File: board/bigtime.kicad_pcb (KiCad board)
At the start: 2 copper layers, 90 x 142 mm, 124 parts, among them IC1 NPIC6C596A, IC2 TPS62152, IC3 25AA02E48, IC4 STM32F407VET6, IC5 KSZ8081RNx, IC6 MAX5969x, IC7 MAX17503, IC8 LDL212DR, J1 RJHSE-538B, J2 MICROUSB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

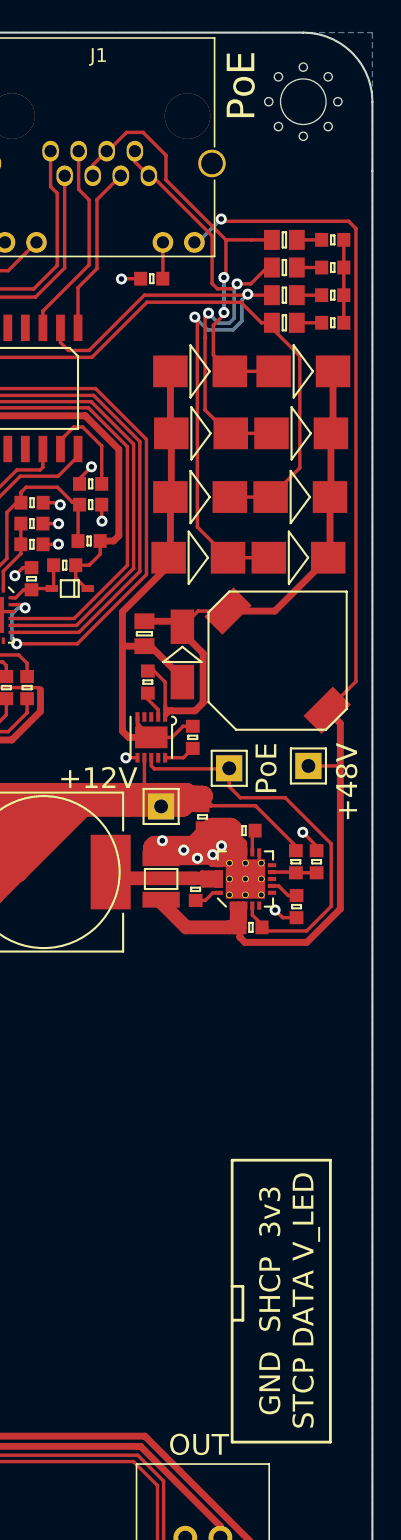
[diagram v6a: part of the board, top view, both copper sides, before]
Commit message: more silk fiddling
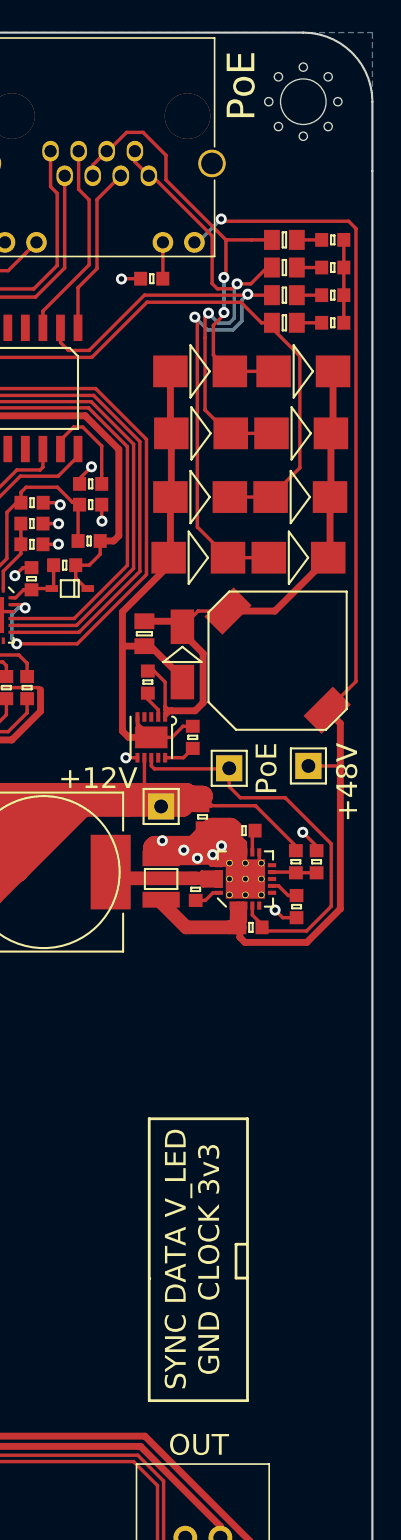
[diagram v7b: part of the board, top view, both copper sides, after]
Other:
- board text added: "SYNC DATA V_LED GND CLOCK 3v3"
- board text removed: "GND SHCP 3v3 STCP DATA V_LED"
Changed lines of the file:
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@@
     (descr "mod. jack, ethernet, 8P8C, RJ45 connector, 2 leds, shielded")
     (tags "RJHSE538X 8P8C RJ45 ethernet jack")
-    (fp_text reference J1 (at 3.49 -6.92) (layer F.SilkS)
+    (fp_text reference J1 (at 3.49 -6.92) (layer F.SilkS) hide
       (effects (font (size 1 1) (thickness 0.15)))
     )
@@
     (effects (font (size 2 2) (thickness 0.3)))
   )
-  (gr_line (start 204.86 112.18) (end 204.89 112.18) (layer F.SilkS) (width 0.2))
-  (gr_line (start 205.63 112.18) (end 204.89 112.18) (layer F.SilkS) (width 0.2))
-  (gr_line (start 205.63 109.73) (end 205.63 112.18) (layer F.SilkS) (width 0.2))
-  (gr_line (start 204.84 109.73) (end 205.63 109.73) (layer F.SilkS) (width 0.2))
-  (gr_line (start 204.84 100.6) (end 204.85 100.6) (layer F.SilkS) (width 0.2))
-  (gr_line (start 211.96 100.6) (end 204.85 100.6) (layer F.SilkS) (width 0.2))
-  (gr_line (start 211.96 121) (end 211.96 100.6) (layer F.SilkS) (width 0.2))
-  (gr_line (start 204.85 121) (end 211.96 121) (layer F.SilkS) (width 0.2))
-  (gr_line (start 204.85 100.65) (end 204.85 121) (layer F.SilkS) (width 0.2))
-  (gr_text "GND  SHCP  3v3\nSTCP DATA V_LED" (at 208.83 110.76 90) (layer F.SilkS)
+  (gr_line (start 198.86 109.18) (end 198.89 109.18) (layer F.SilkS) (width 0.2))
+  (gr_line (start 205.13 106.68) (end 205.87 106.68) (layer F.SilkS) (width 0.2))
+  (gr_line (start 205.13 109.13) (end 205.13 106.68) (layer F.SilkS) (width 0.2))
+  (gr_line (start 205.92 109.13) (end 205.13 109.13) (layer F.SilkS) (width 0.2))
+  (gr_line (start 198.84 97.6) (end 198.85 97.6) (layer F.SilkS) (width 0.2))
+  (gr_line (start 205.96 97.6) (end 198.85 97.6) (layer F.SilkS) (width 0.2))
+  (gr_line (start 205.96 118) (end 205.96 97.6) (layer F.SilkS) (width 0.2))
+  (gr_line (start 198.85 118) (end 205.96 118) (layer F.SilkS) (width 0.2))
+  (gr_line (start 198.85 97.65) (end 198.85 118) (layer F.SilkS) (width 0.2))
+  (gr_text "SYNC DATA V_LED\nGND CLOCK 3v3" (at 202 107.76 90) (layer F.SilkS)
     (effects (font (size 1.5 1.5) (thickness 0.3)))
   )

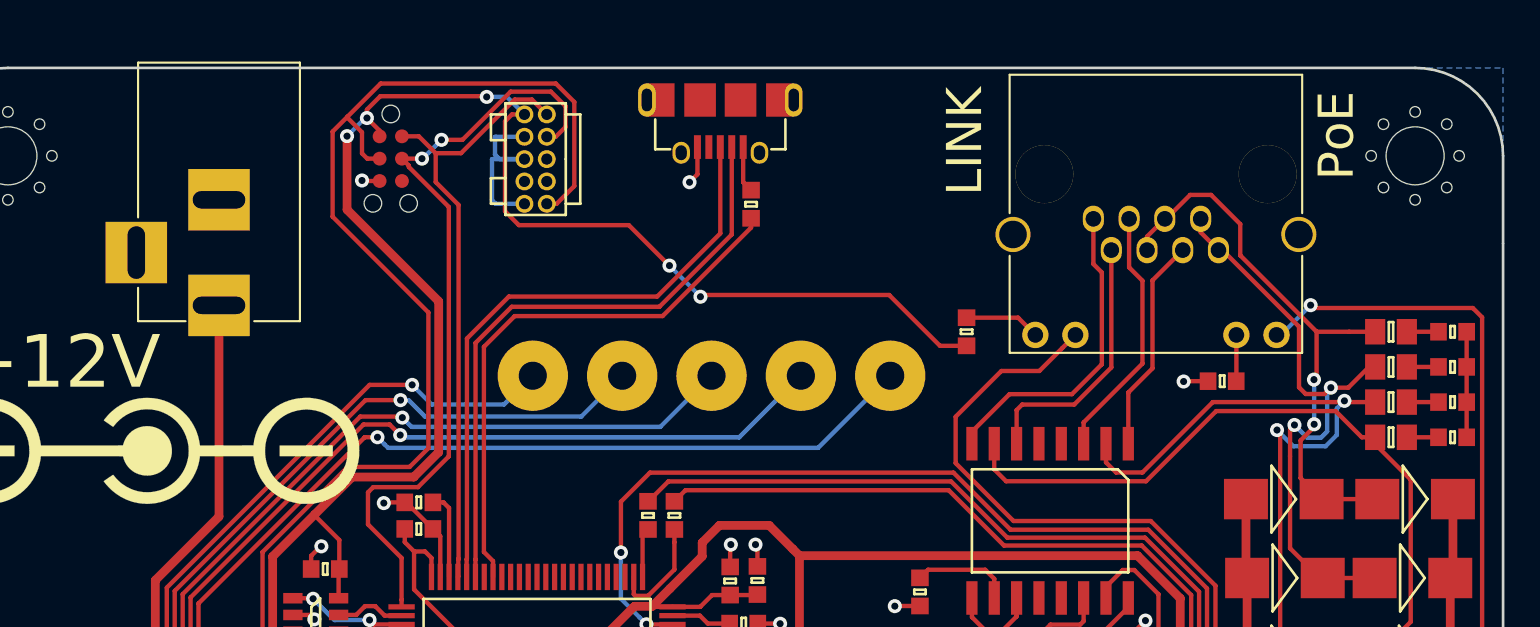
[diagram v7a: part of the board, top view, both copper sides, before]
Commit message: Reduce mask clearance, budge connectors up
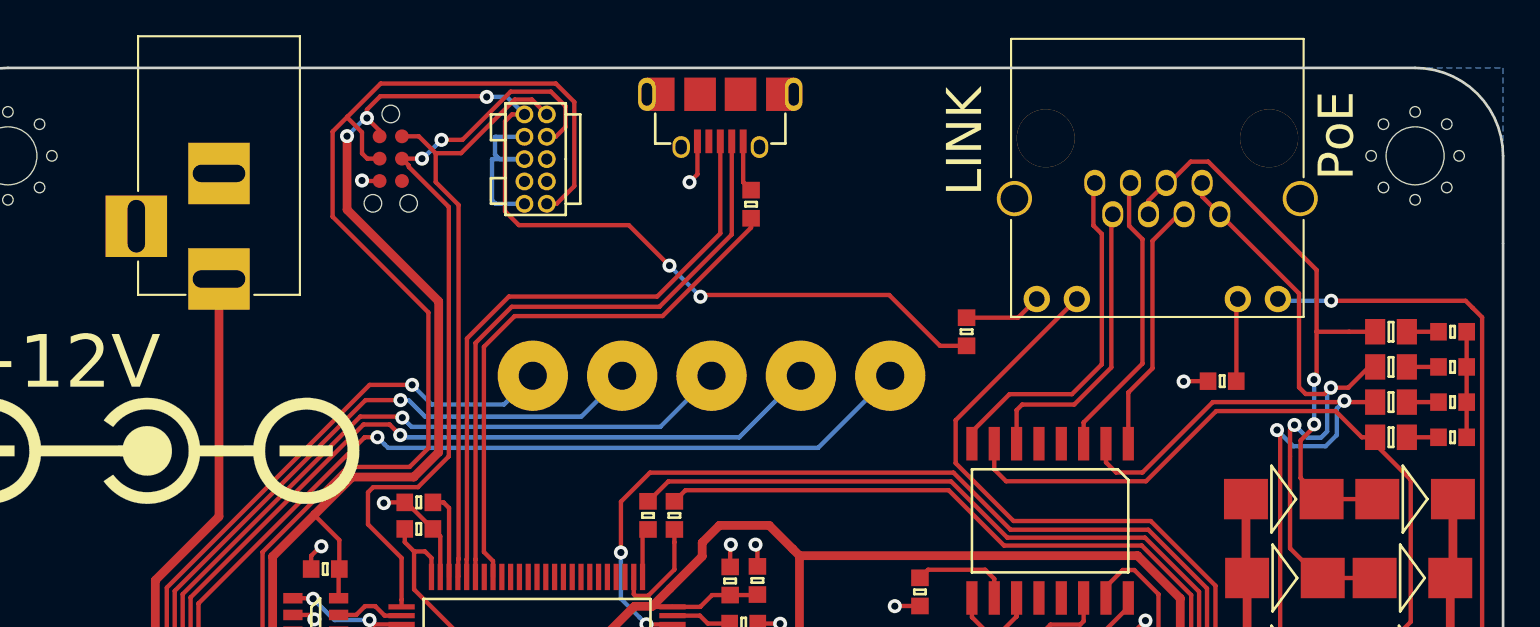
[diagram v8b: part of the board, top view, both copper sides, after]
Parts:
- moved J1 2.04 mm to (191.8, 25.5)
- moved P3 1.50 mm to (142.0, 31.0)
- moved J2 0.32 mm to (170.5, 20.5)
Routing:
- net Net-(J1-Pad6): track 12.3 -> 14.5 mm
- net Net-(J1-Pad2): track 15.8 -> 17.9 mm
- net Net-(J1-Pad11): track 2.63 -> 4.71 mm
- net Net-(J1-Pad3): track 14.5 -> 16.6 mm
- net Net-(J1-Pad1): track 18.7 -> 20.8 mm
- net /ethernet/VB1: track 36.2 -> 38.1 mm
- net +12V: track 250.0 -> 251.5 mm
- net /ethernet/VB2: track 34.1 -> 35.4 mm
- net /ethernet/LINK_LED: track 54.8 -> 55.6 mm
- net +48V: track 91.5 -> 90.9 mm
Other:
- rule pad_to_mask_clearance: 0.2 -> 0
